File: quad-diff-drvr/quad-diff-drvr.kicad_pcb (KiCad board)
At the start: 2 copper layers, 65 x 56 mm, 46 parts, among them J1 Raspberry_Pi_2_3, J2 Conn_01x04, J3 Conn_01x04, J4 Conn_01x04, J5 Conn_01x04, J6 Conn_01x04, U1 INA3221, U2 74LS153, U3 74LS153, U4 74LS153, U5 PCA9555PW, U6 LTC1688

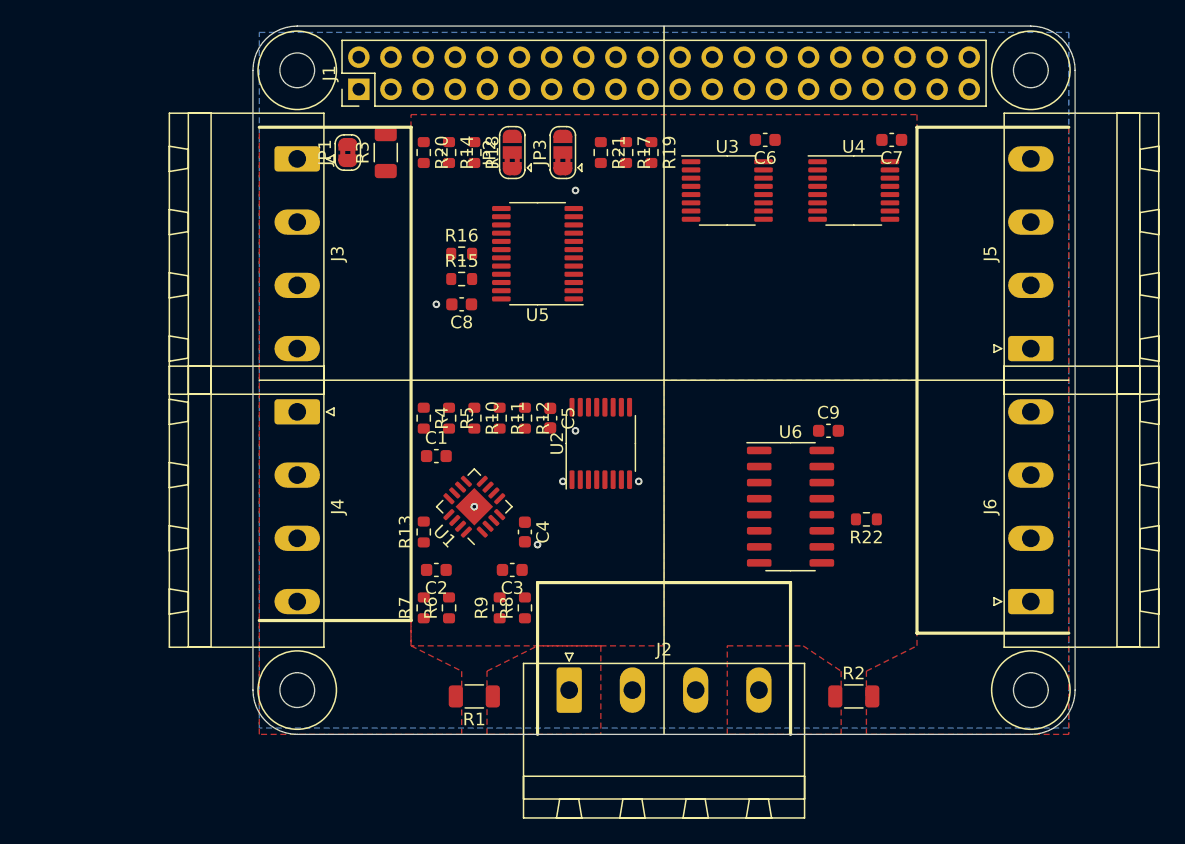
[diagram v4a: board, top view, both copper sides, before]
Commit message: qdd: first pass at routing
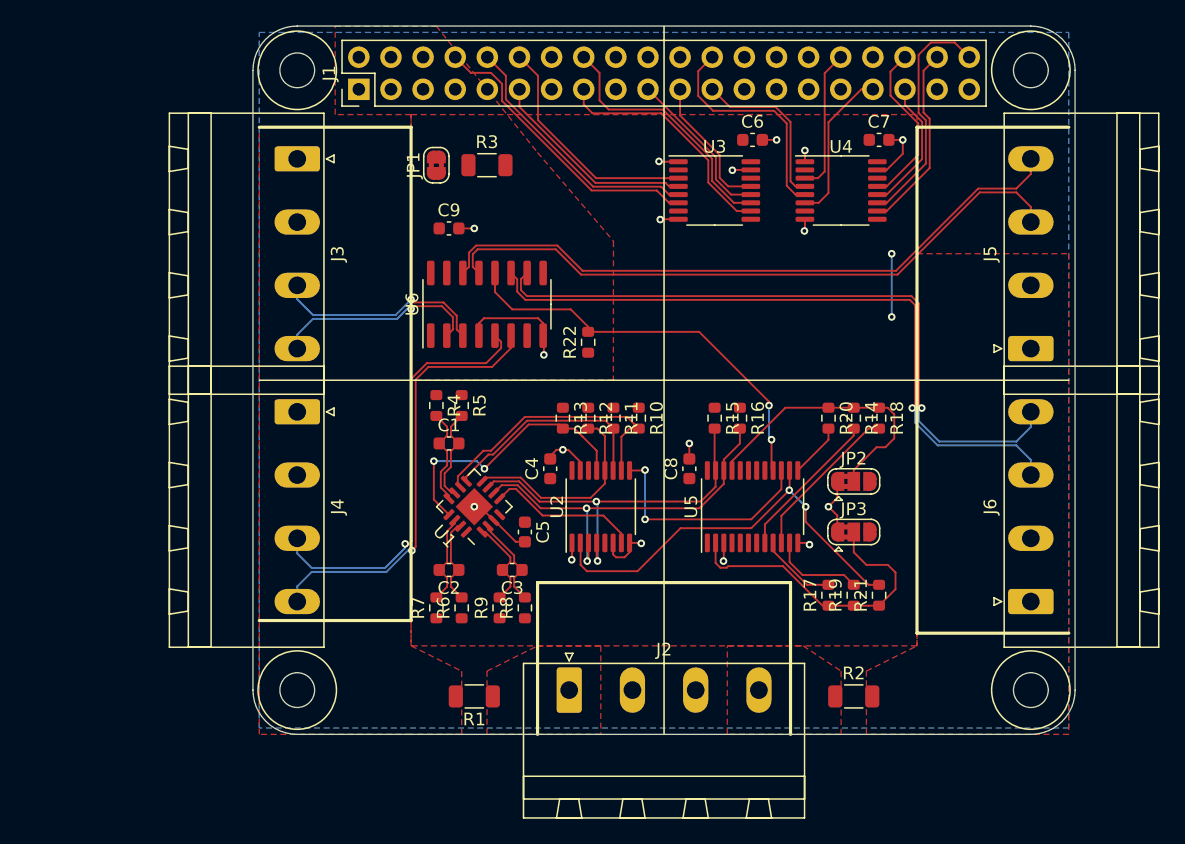
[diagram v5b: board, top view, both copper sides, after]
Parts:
- moved R21 41.3 mm to (117.0, 117.0), turned to 90 degrees
- moved R17 38.5 mm to (113.0, 117.0), turned to 90 degrees
- moved R19 38.5 mm to (115.0, 117.0), turned to 90 degrees
- moved R14 38.3 mm to (115.0, 103.0)
- moved R18 38.3 mm to (117.0, 103.0)
- moved R20 38.3 mm to (113.0, 103.0)
- moved JP3 37.8 mm to (115.0, 112.0), turned to 0 degrees
- moved JP2 37.5 mm to (115.0, 108.0), turned to 0 degrees
- moved C9 34.0 mm to (83.0, 88.0)
- moved U6 28.8 mm to (86.0, 94.0), turned to 90 degrees
- moved U5 26.2 mm to (107.0, 110.0), turned to 90 degrees
- moved R22 26.1 mm to (94.0, 97.0), turned to 90 degrees
- moved R16 25.6 mm to (106.0, 103.0), turned to 270 degrees
- moved R15 22.8 mm to (104.0, 103.0), turned to 270 degrees
- moved C8 22.2 mm to (102.0, 107.0), turned to 90 degrees
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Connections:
- net Net-(C1-Pad1) renamed /IN1+
- net Net-(C1-Pad2) renamed /IN1-
- net Net-(C2-Pad1) renamed /IN2+
- net Net-(C2-Pad2) renamed /IN2-
- net Net-(C3-Pad1) renamed /IN3+
- net Net-(C3-Pad2) renamed /IN3-
- J3 pad 3: /D0+ -> /D0-
- J3 pad 4: /D0- -> /D0+
- J4 pad 3: /D1+ -> /D1-
- J4 pad 4: /D1- -> /D1+
- J5 pad 3: /D2+ -> /D2-
- J5 pad 4: /D2- -> /D2+
- J6 pad 3: /D3+ -> /D3-
- J6 pad 4: /D3- -> /D3+
- U3 pad 12: /SD0 -> /SD2
- U4 pad 12: /SD4 -> /SD11
- U4 pad 13: /SD5 -> /SD8
- U4 pad 3: /SD11 -> /SD4
- U4 pad 5: /SD2 -> /SD0
- U4 pad 6: /SD8 -> /SD5
- U6 pad 1: /D1 -> /D0
- U6 pad 10: /D2+ -> /D3+
- U6 pad 11: /D2- -> /D3-
- U6 pad 13: /D3- -> /D2-
- U6 pad 14: /D3+ -> /D2+
- U6 pad 15: /D3 -> /D2
- U6 pad 2: /D1+ -> /D0+
- U6 pad 3: /D1- -> /D0-
- U6 pad 5: /D0- -> /D1-
- U6 pad 6: /D0+ -> /D1+
- U6 pad 7: /D0 -> /D1
- U6 pad 9: /D2 -> /D3
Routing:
- net /D3-: track 0.00 -> 54.6 mm, vias 0 -> 1
- net /D3+: track 0.00 -> 54.1 mm, vias 0 -> 1
- net /D2+: track 0.00 -> 51.7 mm
- net /D2-: track 0.00 -> 51.2 mm
- net GND: track 0.00 -> 45.1 mm, vias 7 -> 17
- net /D1+: track 0.00 -> 34.6 mm, vias 0 -> 1
- net /D1-: track 0.00 -> 33.9 mm, vias 0 -> 1
- net /PM_A1: track 0.00 -> 33.6 mm, vias 0 -> 2
- net /DEN: track 0.00 -> 32.6 mm, vias 0 -> 2
- net /SCL: track 0.00 -> 30.6 mm, vias 0 -> 2
- net /SDA: track 0.00 -> 30.1 mm, vias 0 -> 2
- net /A1: track 0.00 -> 24.3 mm
- net /SD6: track 0.00 -> 23.2 mm
- net /A0: track 0.00 -> 22.6 mm
- net /PM_PV: track 0.00 -> 21.9 mm
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- added copper zone on F.Cu, net +5V

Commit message: qdd: unsure what got out of sync
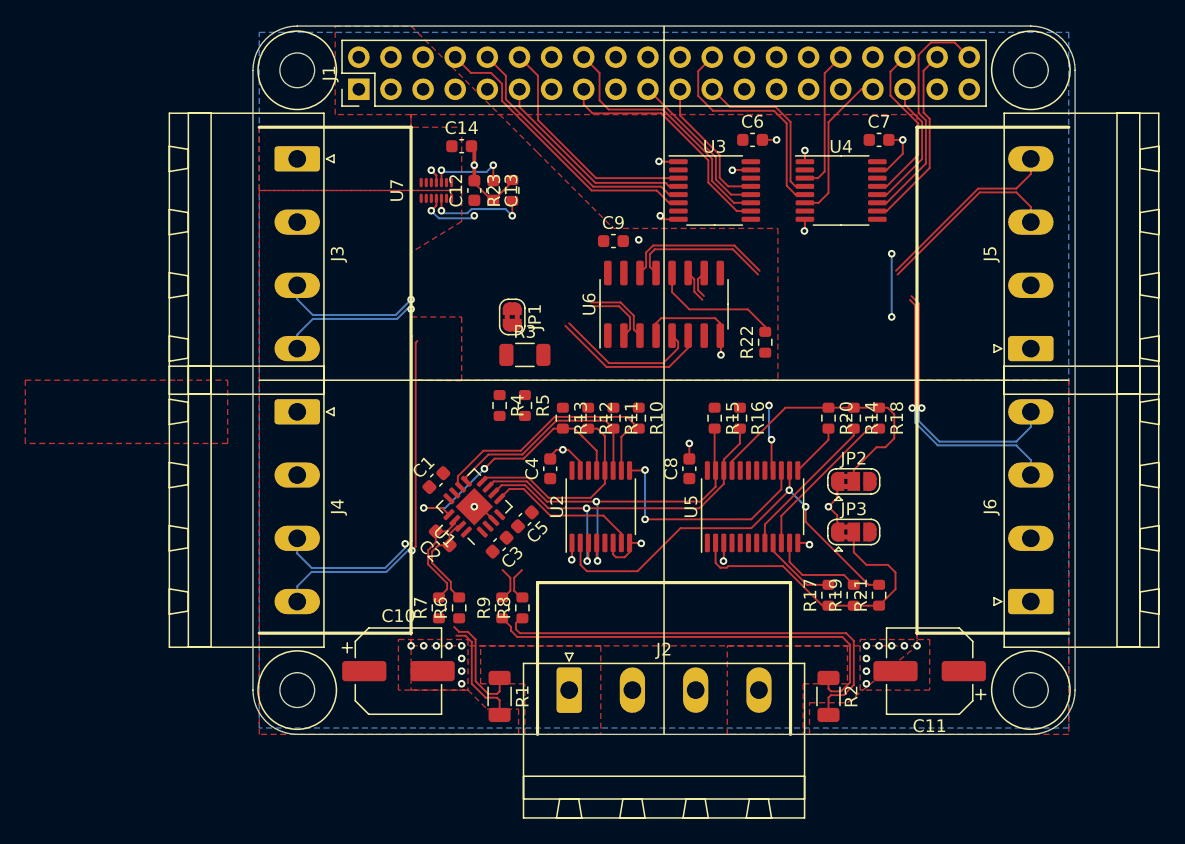
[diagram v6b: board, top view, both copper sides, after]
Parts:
- added C10: 100uF, Capacitor_SMD:CP_Elec_6.3x7.7, F.Cu at (79.0, 123.0)
- added C11: 100uF, Capacitor_SMD:CP_Elec_6.3x7.7, F.Cu at (121.0, 123.0)
- added C12: 100nF, Capacitor_SMD:C_0603_1608Metric, F.Cu at (85.0, 85.0)
- added C13: 4.7nF, Capacitor_SMD:C_0603_1608Metric, F.Cu at (86.5, 85.0)
- added C14: 10uF, Capacitor_SMD:C_0603_1608Metric, F.Cu at (84.0, 81.5)
- added R23: 10k, Resistor_SMD:R_0603_1608Metric, F.Cu at (88.0, 85.0)
- added U7: SLG5NT1581V, octo-pcb:QFN-28_1x3_Pitch0.4mm, F.Cu at (82.0, 85.0)
- moved R3 15.3 mm to (89.0, 98.0)
- moved R22 14.0 mm to (108.0, 97.0)
- moved U6 14.0 mm to (100.0, 94.0)
- moved JP1 13.4 mm to (88.0, 95.0), turned to 270 degrees
- moved C9 13.0 mm to (96.0, 89.0)
- moved R4 5.00 mm to (87.0, 102.0)
- moved R5 5.00 mm to (89.0, 102.0)
- moved C1 3.07 mm to (82.0, 107.9), turned to 45 degrees
- moved C2 2.55 mm to (82.5, 112.5), turned to 135 degrees
- moved C3 2.24 mm to (87.0, 113.0), turned to 225 degrees
- moved R1 2.00 mm to (87.0, 125.0), turned to 270 degrees
- moved R2 2.00 mm to (113.0, 125.0), turned to 270 degrees
- moved C5 1.00 mm to (89.0, 111.0), turned to 225 degrees
- moved R6 0.20 mm to (83.8, 118.0)
- moved R7 0.20 mm to (82.2, 118.0)
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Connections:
- J3 pad 1: /VA -> /VA0
- J4 pad 1: /VA -> (no net)
- U5 pad 4: (no net) -> /VEN0
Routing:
- net /VB: track 0.00 -> 35.5 mm
- net /VB_SENSE: track 0.00 -> 34.5 mm
- net /D3-: track 54.6 -> 24.2 mm
- net /D3+: track 54.1 -> 23.7 mm
- net /D2-: track 51.2 -> 26.1 mm
- net /D2+: track 51.7 -> 26.9 mm
- net /DEN: track 32.6 -> 16.0 mm
- net /VA_SENSE: track 0.00 -> 8.90 mm
- net /VA: track 0.00 -> 8.63 mm
- net /VEN0: track 0.00 -> 8.18 mm, vias 0 -> 2
- net /IN1+: track 7.89 -> 0.00 mm
- net /IN1-: track 7.64 -> 0.00 mm
- net Net-(C13-Pad1): track 0.00 -> 6.57 mm, vias 0 -> 2
- net /D1+: track 34.6 -> 40.8 mm
- net /D1-: track 33.9 -> 39.7 mm
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- added copper zone on F.Cu, net /VA0
- added copper zone on F.Cu, net /VA1
- added copper zone on F.Cu, net GND
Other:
- net class 15A: clearance 0.2 -> 0.15
- net class 4A: clearance 0.2 -> 0.15; trace_width 2 -> 0.15
- net class 9A: clearance 0.2 -> 0.15

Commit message: qdd: stash wip
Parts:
- added C15: 100nF, Capacitor_SMD:C_0603_1608Metric, F.Cu at (59.8, 99.3)
- added C16: 4.7nF, Capacitor_SMD:C_0603_1608Metric, F.Cu at (59.8, 101.8)
- added C17: 10uF, Capacitor_SMD:C_0603_1608Metric, F.Cu at (63.8, 99.3)
- added R24: 10k, Resistor_SMD:R_0603_1608Metric, F.Cu at (63.8, 101.8)
- added U8: SLG5NT1581V, octo-pcb:QFN-28_1x3_Pitch0.4mm, F.Cu at (82.0, 100.0)
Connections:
- J4 pad 1: (no net) -> /VA1
- U5 pad 5: (no net) -> /VEN1
- U7 pad 12: Net-(C13-Pad1) -> (no net)
- U7 pad 3: /VEN0 -> (no net)
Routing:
- net /D1-: track 39.7 -> 22.8 mm
- net /D1+: track 40.8 -> 24.1 mm
- net /VA: vias 0 -> 12
- added copper zone on B.Cu, net /VA

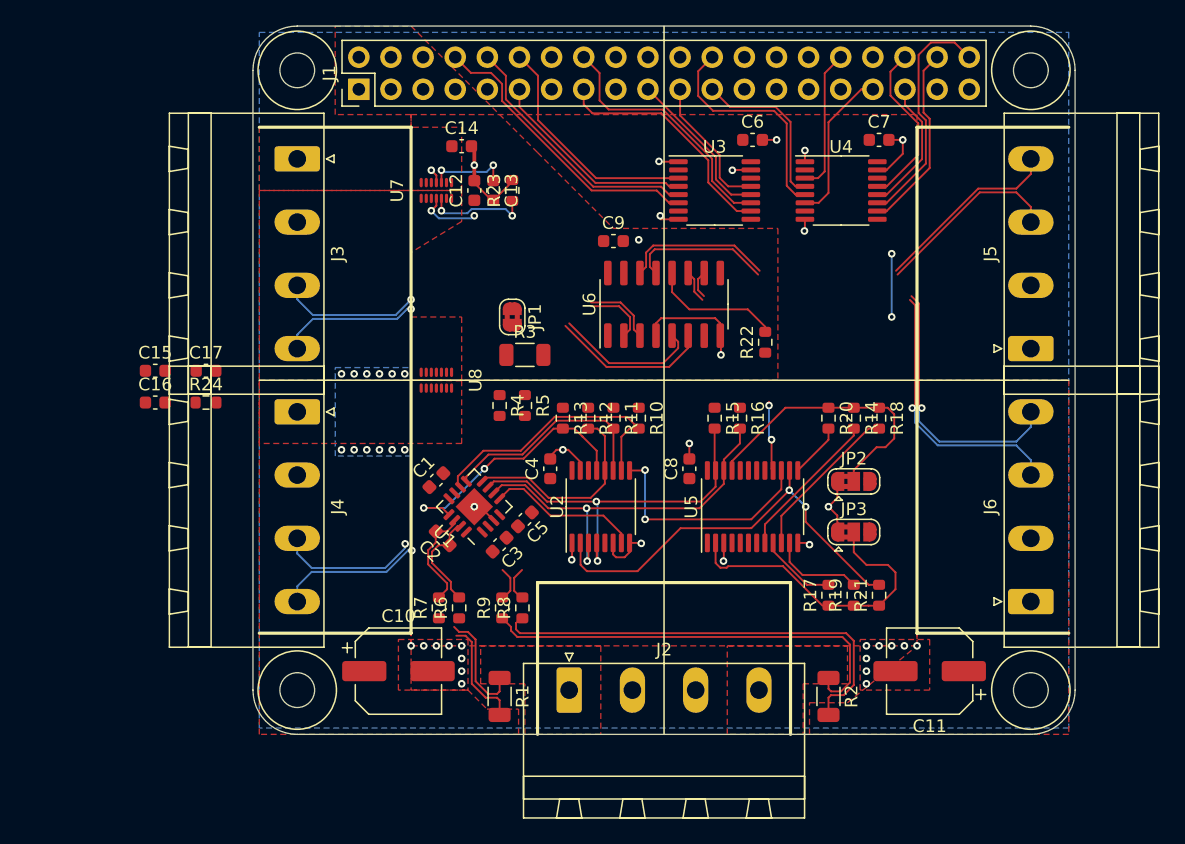
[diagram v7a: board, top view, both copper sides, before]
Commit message: qdd: two high-side switches in
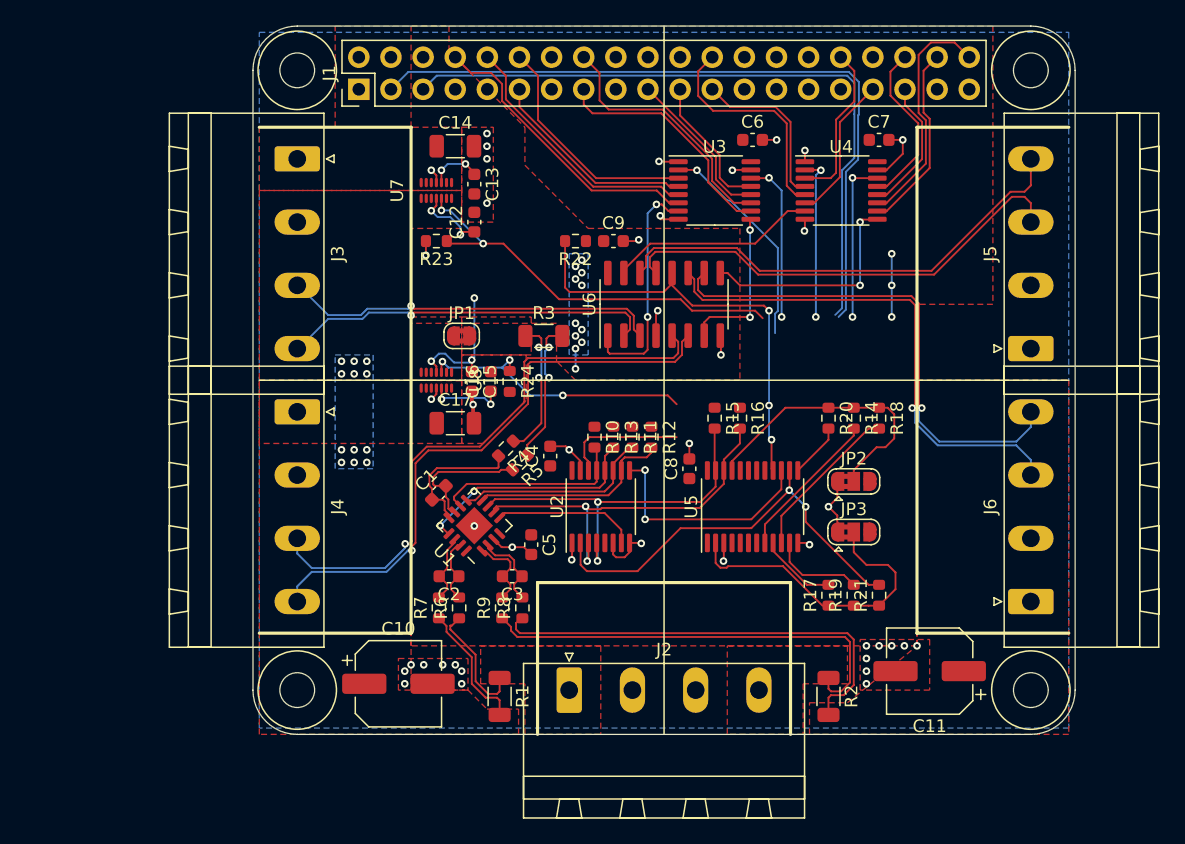
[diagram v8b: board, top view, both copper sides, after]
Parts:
- C14, C17: footprint Capacitor_SMD:C_0603_1608Metric -> Capacitor_SMD:C_1206_3216Metric
- moved C16 26.6 mm to (86.3, 100.1), turned to 90 degrees
- moved C15 25.0 mm to (84.8, 100.1), turned to 270 degrees
- moved R24 24.1 mm to (87.8, 100.1), turned to 270 degrees
- moved C17 20.1 mm to (83.5, 103.4)
- moved R22 17.0 mm to (93.0, 89.0), turned to 180 degrees
- moved R23 7.21 mm to (82.0, 89.0), turned to 180 degrees
- moved R12 5.22 mm to (99.0, 104.5)
- moved R5 4.52 mm to (88.6, 106.5), turned to 225 degrees
- moved JP1 4.27 mm to (84.0, 96.5), turned to 0 degrees
- moved R13 4.27 mm to (96.0, 104.5)
- moved R10 3.81 mm to (94.5, 104.5)
- moved R4 3.44 mm to (87.5, 105.4), turned to 225 degrees
- moved C2 3.04 mm to (83.0, 115.5), turned to 180 degrees
- moved C3 2.69 mm to (88.0, 115.5), turned to 180 degrees
- moved C12 2.50 mm to (85.0, 87.5)
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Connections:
- U2 pad 10: /PM_PV -> /PM_WARN
- U2 pad 12: /PM_WARN -> /PM_TC
- U2 pad 13: /PM_TC -> /PM_PV
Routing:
- net /SDA: track 30.1 -> 86.7 mm
- net /SCL: track 30.6 -> 83.9 mm
- net +5V: track 4.87 -> 29.8 mm, vias 2 -> 18
- net /VEN0: track 8.18 -> 32.8 mm
- net /D1-: track 22.8 -> 46.2 mm
- net /D1+: track 24.1 -> 46.6 mm
- net /VEN1: track 0.00 -> 22.5 mm, vias 0 -> 3
- net /DEN: track 16.0 -> 35.6 mm, vias 2 -> 3
- net /D0: track 0.00 -> 18.4 mm, vias 0 -> 2
- net /D3: track 0.00 -> 17.9 mm, vias 0 -> 2
- net /M0_A1: track 6.12 -> 23.4 mm, vias 0 -> 1
- net /D2: track 0.00 -> 16.5 mm
- net /D3-: track 24.2 -> 40.6 mm
- net /D3+: track 23.7 -> 40.1 mm
- net /D0+: track 16.0 -> 29.5 mm
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- added copper zone on B.Cu, net +5V
- added copper zone on F.Cu, net /5V_SENSE
